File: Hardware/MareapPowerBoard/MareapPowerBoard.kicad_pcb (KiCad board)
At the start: 2 copper layers, 90 x 70 mm, 74 parts, among them J1 XT60PW-M, J10 Comp_Plus_Pin, J11 Comp_Minus_Pin, J12 5VConv_Pin, J13 Batt_Pin, J14 5VUSB_Pin, J15 PowerPins, J2 USB_C_Receptacle_USB2.0_16P, J3 USB_C_MALE, J4 SSD1306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

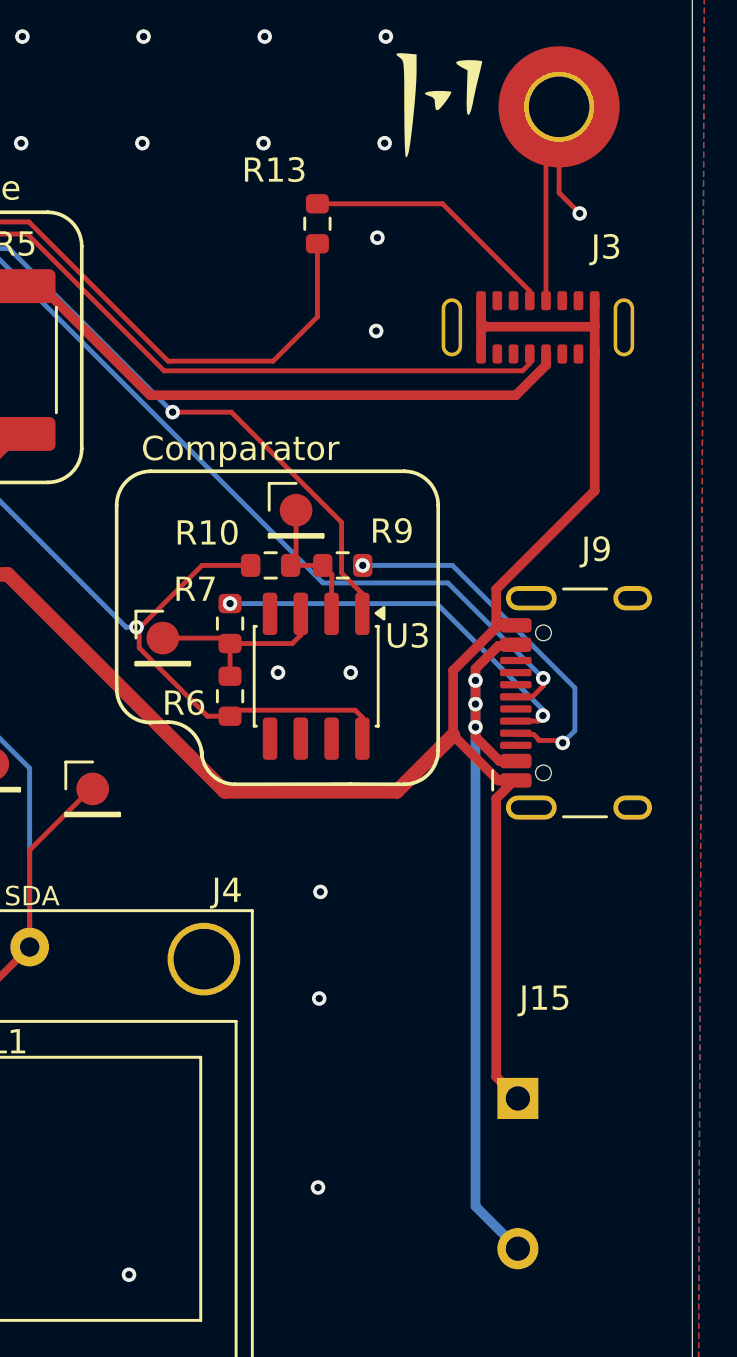
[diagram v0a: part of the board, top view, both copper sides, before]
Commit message: added missing connection and r14 for noise filtering
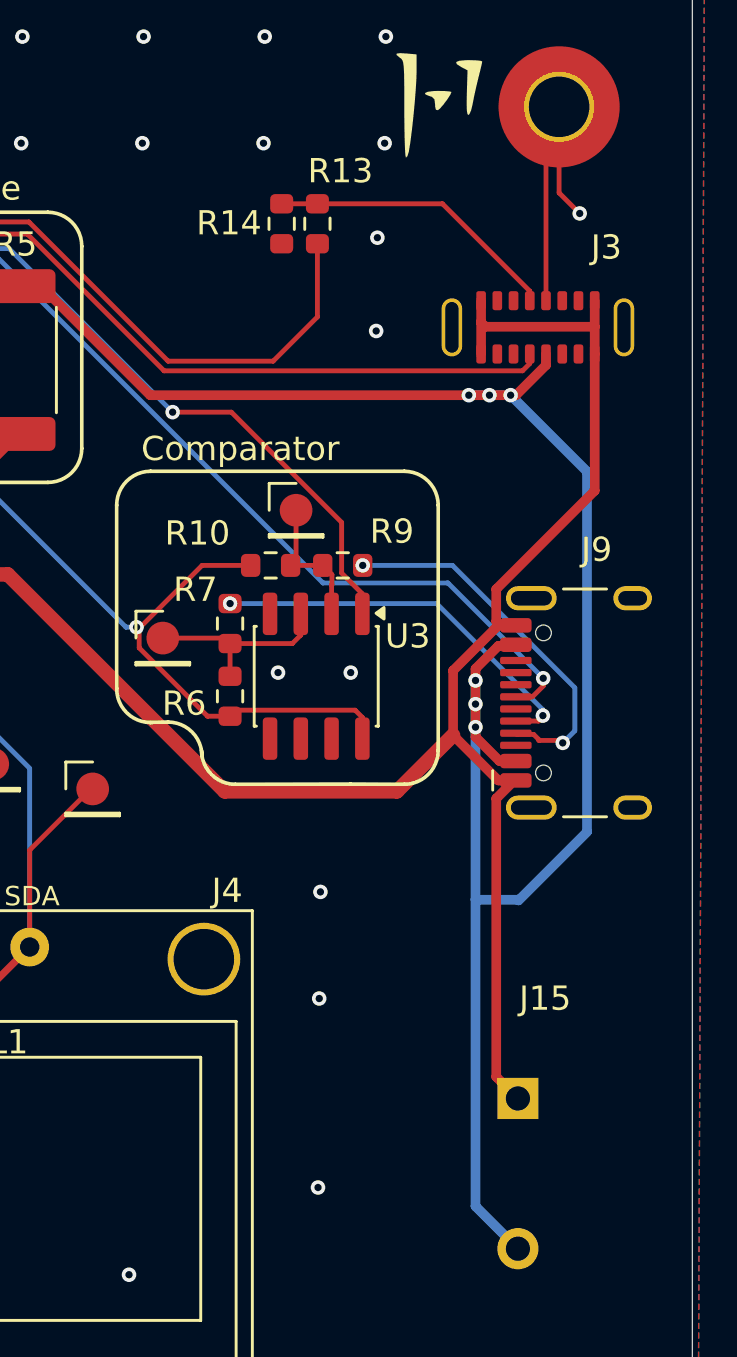
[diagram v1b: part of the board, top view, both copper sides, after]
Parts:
- added R14: 10K, Resistor_SMD:R_0603_1608Metric, F.Cu at (171.6, 82.8)
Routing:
- net +5Vsense: track 57.4 -> 84.2 mm, vias 3 -> 6
- net Net-(J3-D--PadB7): track 10.7 -> 12.1 mm
